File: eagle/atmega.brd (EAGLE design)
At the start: 100 x 80 mm, 66 parts, among them IC1 TO 5V, IC2 LM339D, Q2 16MHz, U1 ATMEGA328P-AU

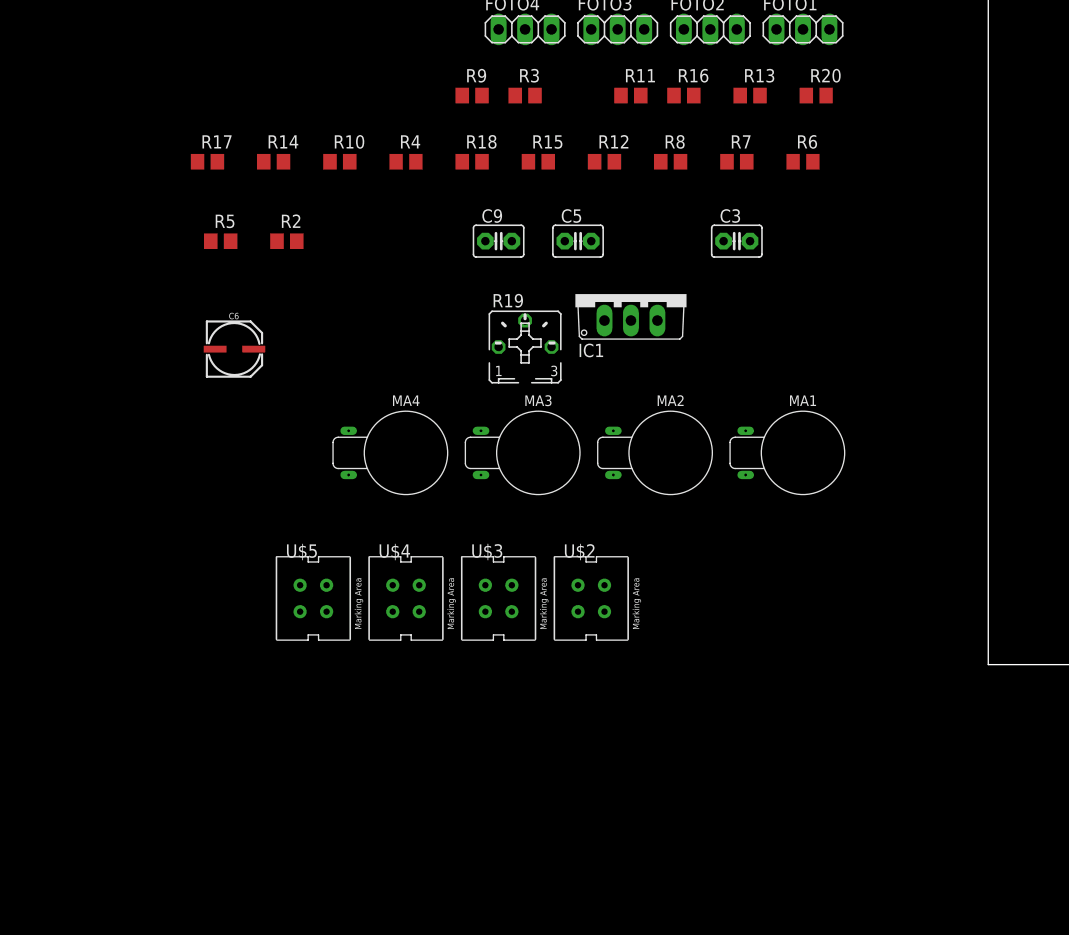
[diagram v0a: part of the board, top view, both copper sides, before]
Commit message: Dodanie mini USB. Dodaj rezystory przed USB, podmień obudowy rezystorów.
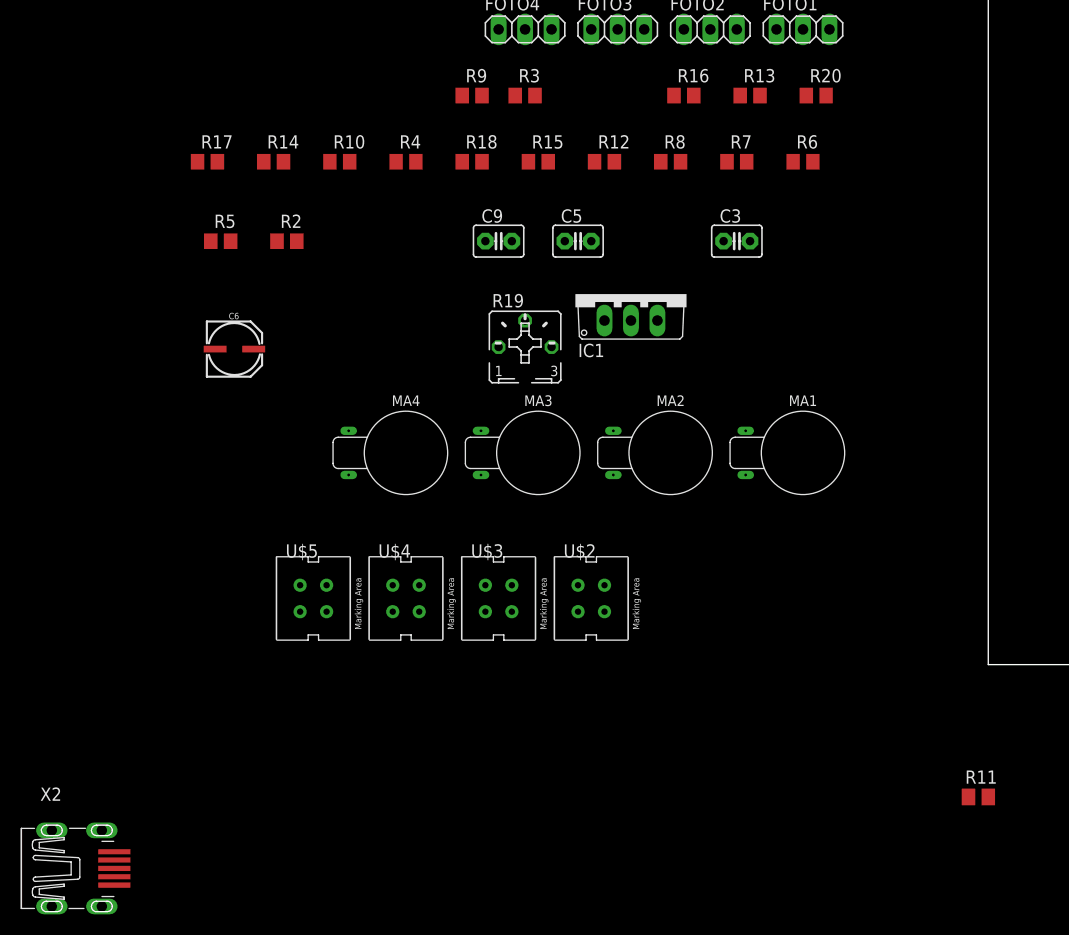
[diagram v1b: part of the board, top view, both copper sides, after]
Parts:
- added X2: MINI-USB_SHIELD5P4-32005-501, con-cypressindustries:32005-501
- R11: device rcl:R0805 -> resistor:M0805
- moved R11 75.1 mm to (-0.95, -12.7)
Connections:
- net N$48 renamed D+
- net N$49 renamed D-
- removed net N$50: U$6.2
- new net N$64: X2.2
- new net N$65: X2.3
- new net N$66: X2.4
- new net N$67: X2.5
- new net USBVCC: U$6.2, X2.1
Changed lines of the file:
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@@
 <attribute name="SPICEPREFIX" value="R" x="-62.23" y="48.26" size="1.778" layer="27" display="off"/>
 </element>
-<element name="R11" library="rcl" library_urn="urn:adsk.eagle:library:334" package="R0805" package3d_urn="urn:adsk.eagle:package:23553/2" value="220" x="-34.29" y="54.61">
-<attribute name="SPICEPREFIX" value="R" x="-34.29" y="54.61" size="1.778" layer="27" display="off"/>
-</element>
+<element name="R11" library="resistor" library_urn="urn:adsk.eagle:library:348" package="M0805" package3d_urn="urn:adsk.eagle:package:26079/1" value="220" x="-0.95" y="-12.7"/>
 <element name="R12" library="rcl" library_urn="urn:adsk.eagle:library:334" package="R0805" package3d_urn="urn:adsk.eagle:package:23553/2" value="220R" x="-36.83" y="48.26">
 <attribute name="SPICEPREFIX" value="R" x="-36.83" y="48.26" size="1.778" layer="27" display="off"/>
@@
 </element>
 <element name="U$6" library="mega32U4" package="TQFP44" value="ATMEGA32U4-AU" x="73.914" y="25.908"/>
+<element name="X2" library="con-cypressindustries" library_urn="urn:adsk.eagle:library:138" package="32005-501" package3d_urn="urn:adsk.eagle:package:6463/1" value="MINI-USB_SHIELD5P4-32005-501" x="-86.868" y="-19.558">
+<attribute name="MF" value="" x="-86.868" y="-19.558" size="1.778" layer="27" display="off"/>
+<attribute name="MPN" value="" x="-86.868" y="-19.558" size="1.778" layer="27" display="off"/>
+<attribute name="OC_FARNELL" value="unknown" x="-86.868" y="-19.558" size="1.778" layer="27" display="off"/>
+<attribute name="OC_NEWARK" value="unknown" x="-86.868" y="-19.558" size="1.778" layer="27" display="off"/>
+</element>
 </elements>
 <signals>
@@
 <wire x1="-24.13" y1="60.96" x2="-15.24" y2="60.96" width="0" layer="19" extent="1-1"/>
 <wire x1="-33.02" y1="60.96" x2="-24.13" y2="60.96" width="0" layer="19" extent="1-1"/>
-<wire x1="-35.24" y1="54.61" x2="-33.02" y2="60.96" width="0" layer="19" extent="1-1"/>
+<wire x1="-1.9" y1="-12.7" x2="-33.02" y2="60.96" width="0" layer="19" extent="1-1"/>
 <wire x1="-41.91" y1="60.96" x2="-33.02" y2="60.96" width="0" layer="19" extent="1-1"/>
 <wire x1="-41.91" y1="67.31" x2="-41.91" y2="60.96" width="0" layer="19" extent="1-1"/>
-<wire x1="-40.64" y1="40.64" x2="-35.24" y2="54.61" width="0" layer="19" extent="1-1"/>
+<wire x1="-40.64" y1="40.64" x2="-1.9" y2="-12.7" width="0" layer="19" extent="1-1"/>
 <wire x1="-36.83" y1="33.02" x2="-40.64" y2="40.64" width="0" layer="19" extent="1-1"/>
 <wire x1="-46.99" y1="30.48" x2="-36.83" y2="33.02" width="0" layer="19" extent="1-1"/>
@@
 <contactref element="LED2" pad="C"/>
 <contactref element="R11" pad="2"/>
-<wire x1="-53.34" y1="68.36" x2="-33.34" y2="54.61" width="0" layer="19" extent="1-1"/>
+<wire x1="-53.34" y1="68.36" x2="0" y2="-12.7" width="0" layer="19" extent="1-1"/>
 </signal>
 <signal name="N$9">
@@
 <contactref element="U$6" pad="5"/>
 </signal>
-<signal name="N$48">
+<signal name="D+">
 <contactref element="U$6" pad="4"/>
 </signal>
-<signal name="N$49">
+<signal name="D-">
 <contactref element="U$6" pad="3"/>
 </signal>
-<signal name="N$50">
+<signal name="USBVCC">
 <contactref element="U$6" pad="2"/>
+<contactref element="X2" pad="1"/>
+<wire x1="68.114" y1="29.108" x2="-83.868" y2="-17.958" width="0" layer="19" extent="1-1"/>
 </signal>
 <signal name="N$51">
@@
 <contactref element="U$6" pad="42"/>
 </signal>
+<signal name="N$64">
+<contactref element="X2" pad="2"/>
+</signal>
+<signal name="N$65">
+<contactref element="X2" pad="3"/>
+</signal>
+<signal name="N$66">
+<contactref element="X2" pad="4"/>
+</signal>
+<signal name="N$67">
+<contactref element="X2" pad="5"/>
+</signal>
 </signals>

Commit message: Podłączenie USB, Początek podłączania do sterownika.
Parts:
- added C10: 1uF, capacitor-wima:C2.5-3
- added R1, R22: 22R, resistor:M0805
- R10, R12, R13, R14, R15, R16, R17, R18, R2, R20, R21, R3, R4, R5, R6, R7, R8, R9: device rcl:R0805 -> resistor:M0805
- ZWORKA: device rcl:P0613V -> rcl:0204/5
- moved R7 288.3 mm to (-0.95, -239.1)
- moved R8 276.3 mm to (-0.95, -226.4)
- moved R5 264.5 mm to (-0.95, -213.7)
- moved R2 250.6 mm to (-0.95, -201.0)
- moved R20 243.4 mm to (-0.95, -188.3)
- moved R17 235.8 mm to (-0.95, -175.6)
- moved R18 216.7 mm to (-0.95, -162.9)
- moved R16 206.8 mm to (-0.95, -150.2)
- moved R14 197.7 mm to (-0.95, -137.5)
- moved R15 178.1 mm to (-0.95, -124.8)
- moved R13 168.2 mm to (-0.95, -112.1)
- moved R10 159.9 mm to (-0.95, -99.4)
- moved R12 139.7 mm to (-0.95, -86.7)
- moved R9 137.5 mm to (-0.95, -74.0)
- moved R4 122.6 mm to (-0.95, -61.3)
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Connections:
- removed net N$14: U$6.29
- removed net N$15: U$6.30
- removed net N$17: U$6.31
- removed net N$18: U$6.32
- removed net N$27: U$6.25
- removed net N$34: U$6.26
- removed net N$35: U$6.27
- removed net N$45: U$6.7
- removed net N$46: U$6.6
- removed net N$47: U$6.5
- removed net N$58: U$6.15
- removed net N$60: U$6.14
- removed net N$64: X2.2
- removed net N$66: X2.4
- removed net N$67: X2.5
- removed net VCC_2: U1.4
- new net N$49: R1.2, X2.2
- new net UCAP: C10.2, U$6.6
- new net UGND: C10.1, U$6.5, X2.5
- new net VBUS: U$6.7, X2.4
- net AIN1: now also U$6.26
- net AIN2: now also U$6.25
- net BIN1: now also U$6.30
- net BIN2: now also U$6.31
- net D+: now also R22.1
- net D-: now also R1.1
- net GND: now also U$6.15
- net N$65: now also R22.2
- net PWMA: now also U$6.27
- net PWMB: now also U$6.32
- net STBY: now also U$6.29
- net VCC: now also U$6.14, U1.4

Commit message: Usunąłem ATmega32U
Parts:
- removed C10: 1uF, capacitor-wima:C2.5-3
- removed R1, R22: 22R, resistor:M0805
- removed U$6: ATMEGA32U4-AU, mega32U4:TQFP44
- removed X2: MINI-USB_SHIELD5P4-32005-501, con-cypressindustries:32005-501
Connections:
- removed net D+: R22.1, U$6.4
- removed net D-: R1.1, U$6.3
- removed net N$11: U$6.10
- removed net N$12: U$6.11
- removed net N$13: U$6.28
- removed net N$16: U$6.12
- removed net N$19: U$6.18
- removed net N$22: U$6.19
- removed net N$24: U$6.20
- removed net N$25: U$6.21
- removed net N$33: U$6.22
- removed net N$37: U$6.33
- removed net N$38: U$6.1
- removed net N$39: U$6.41
- removed net N$4: U$6.8
- removed net N$40: U$6.40
- removed net N$41: U$6.39
- removed net N$42: U$6.38
- removed net N$43: U$6.37
- removed net N$44: U$6.36
- removed net N$49: R1.2, X2.2
- removed net N$5: U$6.9
- removed net N$51: U$6.16
- removed net N$52: U$6.17
- removed net N$53: U$6.44
- removed net N$54: U$6.24
- removed net N$55: U$6.43
- removed net N$56: U$6.35
- removed net N$57: U$6.23
- removed net N$59: U$6.13
- removed net N$61: U$6.34
- removed net N$62: U$6.42
- removed net N$65: R22.2, X2.3
- removed net UCAP: C10.2, U$6.6
- removed net UGND: C10.1, U$6.5, X2.5
- removed net USBVCC: U$6.2, X2.1
- removed net VBUS: U$6.7, X2.4
- net AIN1: no longer U$6.26
- net AIN2: no longer U$6.25
- net BIN1: no longer U$6.30
- net BIN2: no longer U$6.31
- net GND: no longer U$6.15
- net PWMA: no longer U$6.27
- net PWMB: no longer U$6.32
- net STBY: no longer U$6.29
- net VCC: no longer U$6.14

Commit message: Podłączenie wszystkiego zakończone, wystarczy tylko obawić się nad estetyką
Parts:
- removed ZWORKA: (no value), rcl:0204/5
- added DRILEGEND: (no value), drilegend:DRILEGEND
- R11: value 220 -> 220R
- moved R7 298.1 mm to (21.3, 58.2)
- moved R8 289.1 mm to (20.9, 61.9)
- moved R5 279.0 mm to (20.6, 64.4)
- moved R2 270.5 mm to (20.3, 68.6)
- moved R20 222.0 mm to (38.0, 30.2), turned to 180 degrees
- moved R17 205.6 mm to (54.0, 22.5), turned to 270 degrees
- moved R18 194.1 mm to (56.3, 22.5), turned to 270 degrees
- moved R16 176.5 mm to (51.7, 18.2), turned to 270 degrees
- moved R14 170.8 mm to (58.6, 22.5), turned to 270 degrees
- moved R15 159.8 mm to (60.9, 22.5), turned to 270 degrees
- moved C6 157.6 mm to (85.1, 25.7), turned to 180 degrees
- moved R10 149.2 mm to (58.5, 37.4), turned to 90 degrees
- moved R13 143.8 mm to (48.9, 22.8), turned to 270 degrees
- moved VOLTAGE 140.3 mm to (93.9, 37.3)
- moved LED2 140.1 mm to (85.5, 48.0), turned to 90 degrees
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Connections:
- removed net 7.4V: C3.2, IC1.3, VOLTAGE.1
- removed net N$31: C6.-, C9.1
- removed net RESET3: R21.1, ZWORKA.2
- removed net V+: IC2.3
- new net 5: R8.2
- new net 55: R7.2
- new net 555: R2.2
- new net 5555: R5.2
- new net N$12: U$4.E, U$4.K
- new net N$14: U$3.E, U$3.K
- new net N$15: U$5.E, U$5.K
- new net N$4: U$2.E, U$2.K
- net GND: now also C6.-, C9.1, U1.5; no longer U$2.E, U$2.K, U$3.E, U$3.K, U$4.E, U$4.K, U$5.E, U$5.K, U1.21
- net KO1: now also U1.32; no longer U1.2
- net KO2: now also U1.31; no longer U1.1
- net KO3: now also U1.2; no longer U1.31
- net KO4: now also U1.1; no longer U1.32
- net RESET1: now also R21.1; no longer ZWORKA.1
- net VCC: now also IC2.3; no longer R2.2, R5.2, R7.2, R8.2
- net VZ: now also C3.2, IC1.3, VOLTAGE.1
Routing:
- net VCC: track 19.2 -> 267.3 mm, vias 0 -> 2
- net GND: track 23.8 -> 223.2 mm, vias 0 -> 6
- net POT: track 0.00 -> 27.3 mm, vias 0 -> 2
- net CO6: track 7.03 -> 33.5 mm
- net CO5: track 5.21 -> 27.5 mm
- net KOM4: track 0.00 -> 22.1 mm
- net KO4: track 0.00 -> 22.0 mm
- net VZ: track 7.88 -> 28.3 mm, vias 0 -> 2
- net KOM1: track 0.00 -> 20.0 mm
- net KOM3: track 0.00 -> 20.0 mm
- net KO1: track 0.00 -> 19.7 mm
- net KOM2: track 0.00 -> 18.8 mm
- net KO3: track 0.00 -> 18.6 mm
- net CO4: track 5.32 -> 22.0 mm
- net CO1: track 15.5 -> 30.1 mm
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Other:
- board size 100 x 80 mm -> 82.4 x 66 mm
- board text added: "01-16"
- board text added: "LAYER-STACK"

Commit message: zapomiałem co się działo
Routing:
- net GND: track 223.2 -> 254.2 mm
- net KO2: track 12.6 -> 14.5 mm
- net PWMB: track 20.7 -> 21.3 mm
- added copper zone on layer 1, net N$5
